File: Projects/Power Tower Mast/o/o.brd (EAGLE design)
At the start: 15.2 x 21.8 mm, 29 parts

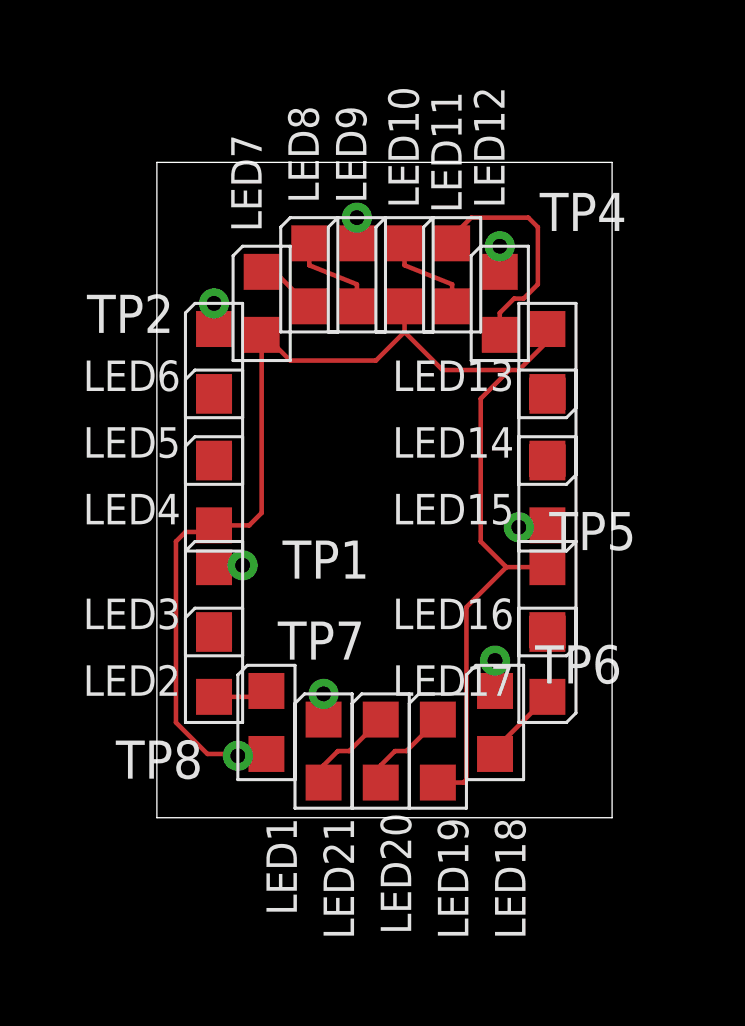
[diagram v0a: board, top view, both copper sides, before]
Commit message: updated with extra vias and panelized
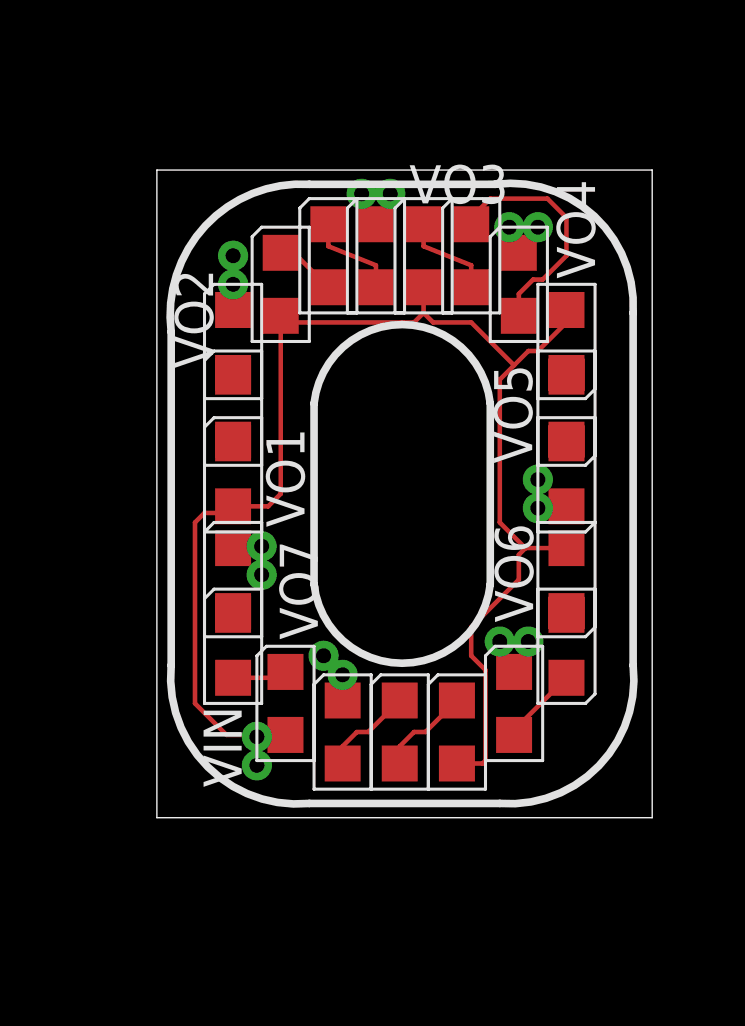
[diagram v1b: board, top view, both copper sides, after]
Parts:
- removed TP1, TP2, TP3, TP4, TP5, TP6, TP7, TP8: (no value), CyberRailGuru:P1-20
- added VIN, VIN1, VO1, VO10, VO11, VO12, VO13, VO14, VO2, VO3, VO4, VO5, VO6, VO7, VO8, VO9: (no value), CyberRailGuru:P1-20
- moved LED7 0.90 mm to (4.13, 17.8)
- moved LED10 0.90 mm to (8.89, 18.7)
- moved LED11 0.90 mm to (10.5, 18.7)
- moved LED12 0.90 mm to (12.1, 17.8)
- moved LED8 0.90 mm to (5.71, 18.7)
- moved LED9 0.90 mm to (7.30, 18.7)
- moved LED1 0.90 mm to (4.29, 3.81)
- moved LED18 0.90 mm to (11.9, 3.81)
- moved LED2 0.90 mm to (2.54, 5.71)
- moved LED3 0.90 mm to (2.54, 7.94)
- moved LED4 0.90 mm to (2.54, 11.4)
- moved LED5 0.90 mm to (2.54, 13.7)
- moved LED6 0.90 mm to (2.54, 15.9)
- moved LED13 0.90 mm to (13.7, 15.9)
- moved LED14 0.90 mm to (13.7, 13.7)
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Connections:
- removed net VIN2: LED1.A, LED10.A, LED13.A, LED16.A, LED19.A, LED4.A, LED7.A, TP8.TP
- removed net VOUT10: LED12.C, TP4.TP
- removed net VOUT11: LED15.C, TP5.TP
- removed net VOUT12: LED18.C, TP6.TP
- removed net VOUT13: LED21.C, TP7.TP
- removed net VOUT8: LED6.C, TP2.TP
- removed net VOUT9: LED9.C, TP3.TP
- new net VIN: LED1.A, LED10.A, LED13.A, LED16.A, LED19.A, LED4.A, LED7.A, VIN.TP, VIN1.TP
- new net VOUT1: LED3.C, VO1.TP, VO8.TP
- new net VOUT2: LED6.C, VO2.TP, VO9.TP
- new net VOUT3: LED9.C, VO10.TP, VO3.TP
- new net VOUT4: LED12.C, VO11.TP, VO4.TP
- new net VOUT5: LED15.C, VO12.TP, VO5.TP
- new net VOUT6: LED18.C, VO13.TP, VO6.TP
- net VOUT7: now also LED21.C, VO14.TP, VO7.TP; no longer LED3.C, TP1.TP
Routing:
- net VIN: track 0.00 -> 49.1 mm
- net VIN2: track 48.5 -> 0.00 mm
- net VOUT3: track 0.00 -> 2.44 mm
- net VOUT6: track 0.00 -> 2.44 mm
- net VOUT4: track 0.00 -> 2.12 mm
- net VOUT1: track 0.00 -> 1.97 mm
- net VOUT5: track 0.00 -> 1.93 mm
- net VOUT2: track 0.00 -> 1.81 mm
- net VOUT11: track 0.98 -> 0.00 mm
- net VOUT9: track 0.86 -> 0.00 mm
- net VOUT8: track 0.86 -> 0.00 mm
- net VOUT13: track 0.86 -> 0.00 mm
- net VOUT10: track 0.86 -> 0.00 mm
- net VOUT7: track 0.98 -> 1.75 mm
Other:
- board size 15.2 x 21.8 mm -> 16.5 x 21.6 mm

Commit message: fixed ratio for all letters; continued to update layouts
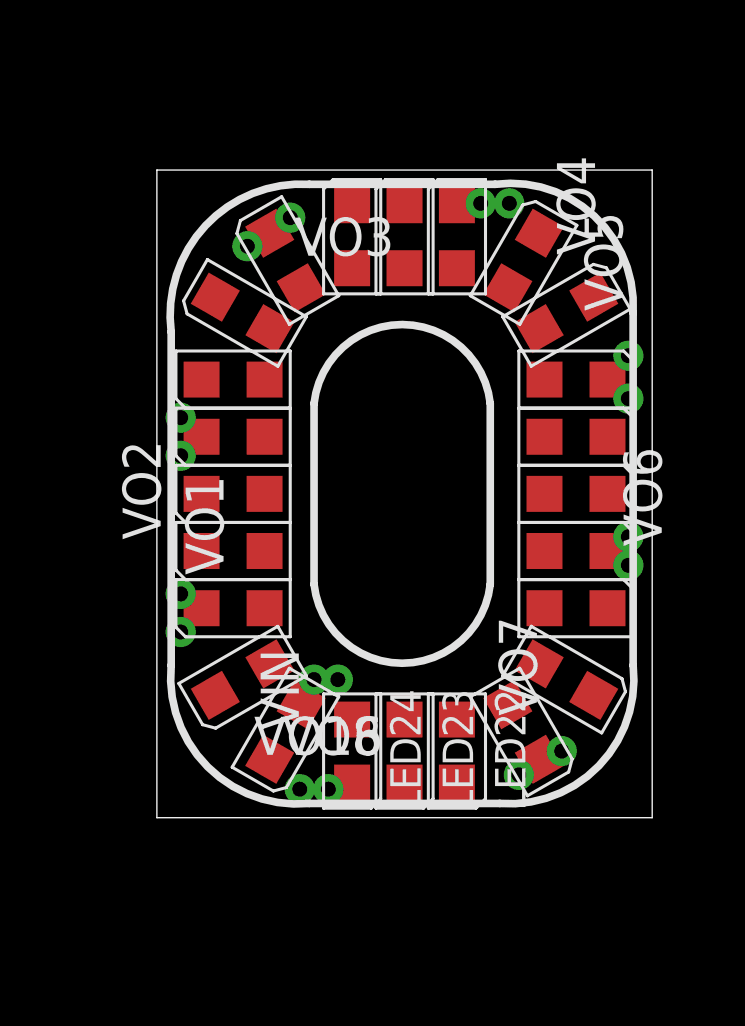
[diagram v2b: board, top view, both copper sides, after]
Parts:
- added LED22, LED23, LED24: (no value), CyberRailGuru:LED_0805
- added VO15, VO16: (no value), CyberRailGuru:P1-20
- moved VO9 12.7 mm to (0.79, 6.19)
- moved VO14 10.9 mm to (15.7, 9.37)
- moved VO10 10.2 mm to (0.79, 13.3)
- moved VO12 9.40 mm to (10.8, 20.5)
- moved VO13 8.76 mm to (15.7, 14.0)
- moved VO11 8.26 mm to (4.45, 20.0)
- moved VO7 7.73 mm to (13.5, 2.22)
- moved VO8 7.48 mm to (5.71, 0.95)
- moved LED21 6.03 mm to (12.2, 2.86), turned to 210 degrees
- moved VO2 5.98 mm to (0.79, 12.1)
- moved VO5 5.91 mm to (15.7, 15.4)
- moved LED20 5.82 mm to (13.7, 4.60), turned to 240 degrees
- moved LED19 5.73 mm to (14.0, 6.99), turned to 270 degrees
- moved LED18 5.48 mm to (14.0, 8.89), turned to 270 degrees
- moved LED17 5.09 mm to (14.0, 10.8), turned to 270 degrees
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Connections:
- new net N$1: LED22.C, LED23.A
- new net N$2: LED23.C, LED24.A
- new net N$5: LED24.C, VO16.TP, VO8.TP
- net VIN: now also LED22.A
- net VOUT1: now also VO9.TP; no longer VO8.TP
- net VOUT2: now also VO10.TP; no longer VO9.TP
- net VOUT3: now also VO11.TP; no longer VO10.TP
- net VOUT4: now also VO12.TP; no longer VO11.TP
- net VOUT5: now also VO13.TP; no longer VO12.TP
- net VOUT6: now also VO14.TP; no longer VO13.TP
- net VOUT7: now also VO15.TP; no longer VO14.TP
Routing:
- net VIN: track 49.1 -> 0.00 mm
- net N$15: track 8.04 -> 0.00 mm
- net N$11: track 3.17 -> 0.00 mm
- net N$16: track 3.17 -> 0.00 mm
- net N$28: track 3.11 -> 0.00 mm
- net N$27: track 3.11 -> 0.00 mm
- net N$23: track 2.63 -> 0.00 mm
- net VOUT3: track 2.44 -> 0.00 mm
- net VOUT6: track 2.44 -> 0.00 mm
- net VOUT4: track 2.12 -> 0.00 mm
- net N$12: track 2.06 -> 0.00 mm
- net VOUT1: track 1.97 -> 0.00 mm
- net VOUT5: track 1.93 -> 0.00 mm
- net N$4: track 1.83 -> 0.00 mm
- net VOUT2: track 1.81 -> 0.00 mm
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
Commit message: final updates before fab.  added new letters for future projects.
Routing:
- net VIN: track 0.00 -> 50.7 mm, vias 0 -> 7
- net N$20: track 0.00 -> 3.67 mm
- net N$3: track 0.00 -> 3.59 mm
- net N$19: track 0.00 -> 3.52 mm
- net N$4: track 0.00 -> 3.41 mm
- net N$16: track 0.00 -> 3.07 mm
- net N$28: track 0.00 -> 3.05 mm
- net N$11: track 0.00 -> 2.99 mm
- net N$27: track 0.00 -> 2.99 mm
- net N$12: track 0.00 -> 2.98 mm
- net N$24: track 0.00 -> 2.89 mm
- net N$23: track 0.00 -> 2.89 mm
- net N$8: track 0.00 -> 2.89 mm
- net N$7: track 0.00 -> 2.89 mm
- net N$15: track 0.00 -> 2.82 mm
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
